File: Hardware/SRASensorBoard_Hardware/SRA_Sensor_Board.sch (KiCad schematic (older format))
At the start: 12 parts, among them U1 OKI-78SR-5_1.5-W36H-C, U2 OKI-78SR-3.3_1.5-W36H-C

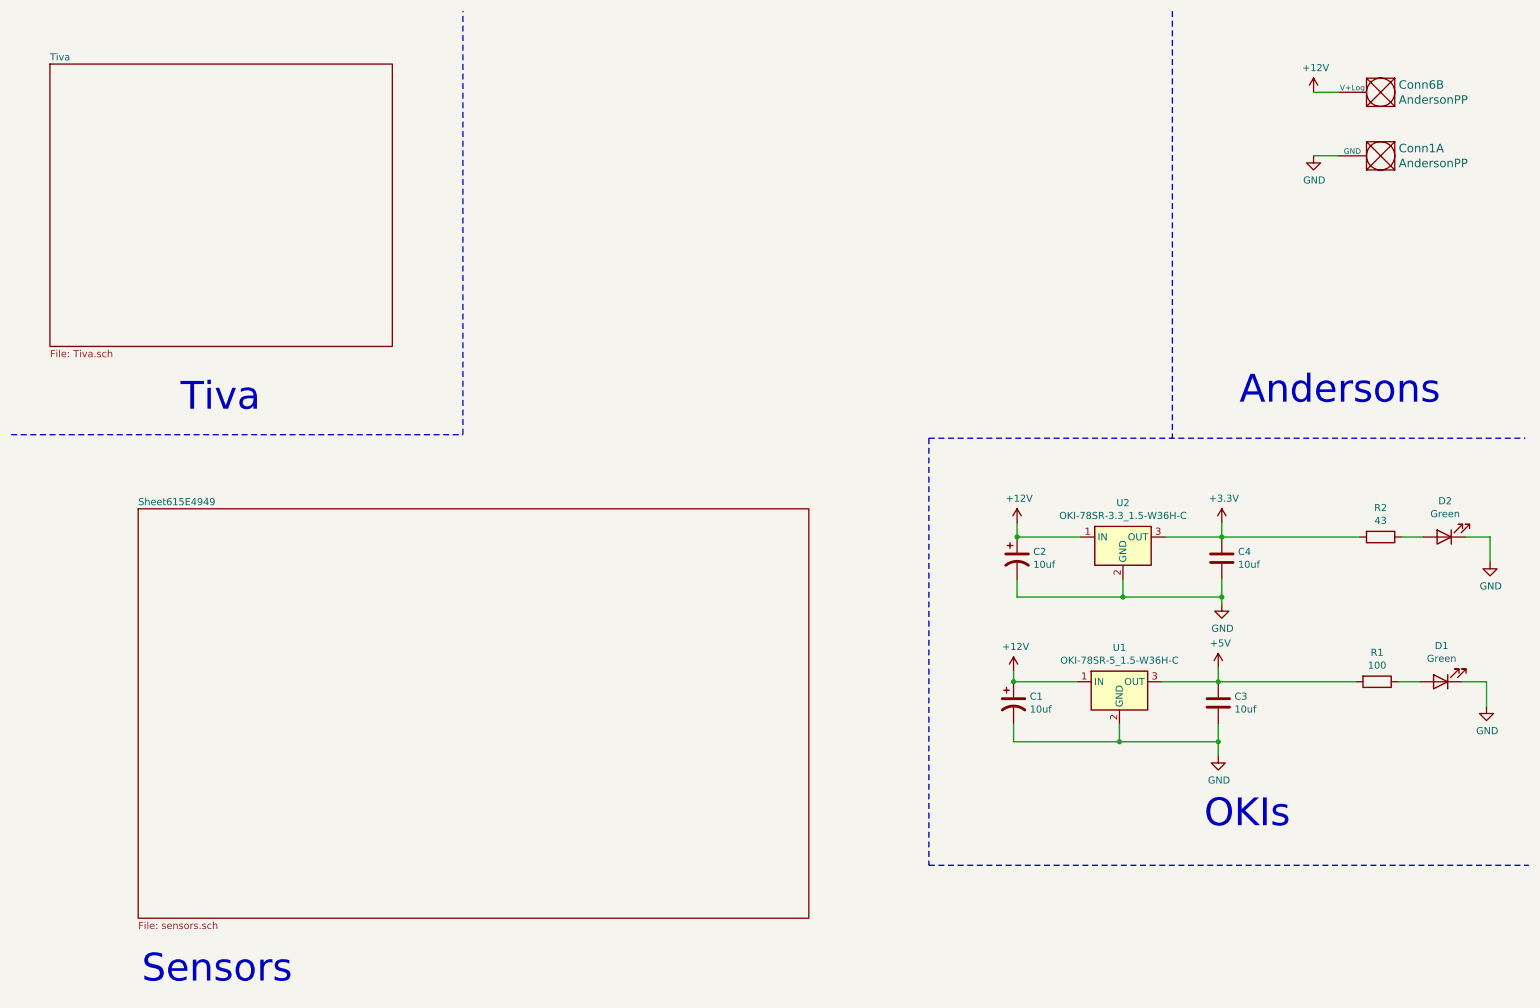
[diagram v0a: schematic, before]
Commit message: Science CDR changes
Changed NO to NO2, removed NH3 data lines for analog output and changed power to 5v, added 3 laser and photodiode pairs (mosfet not determined), added uv and lights connectors, updated tiva pins
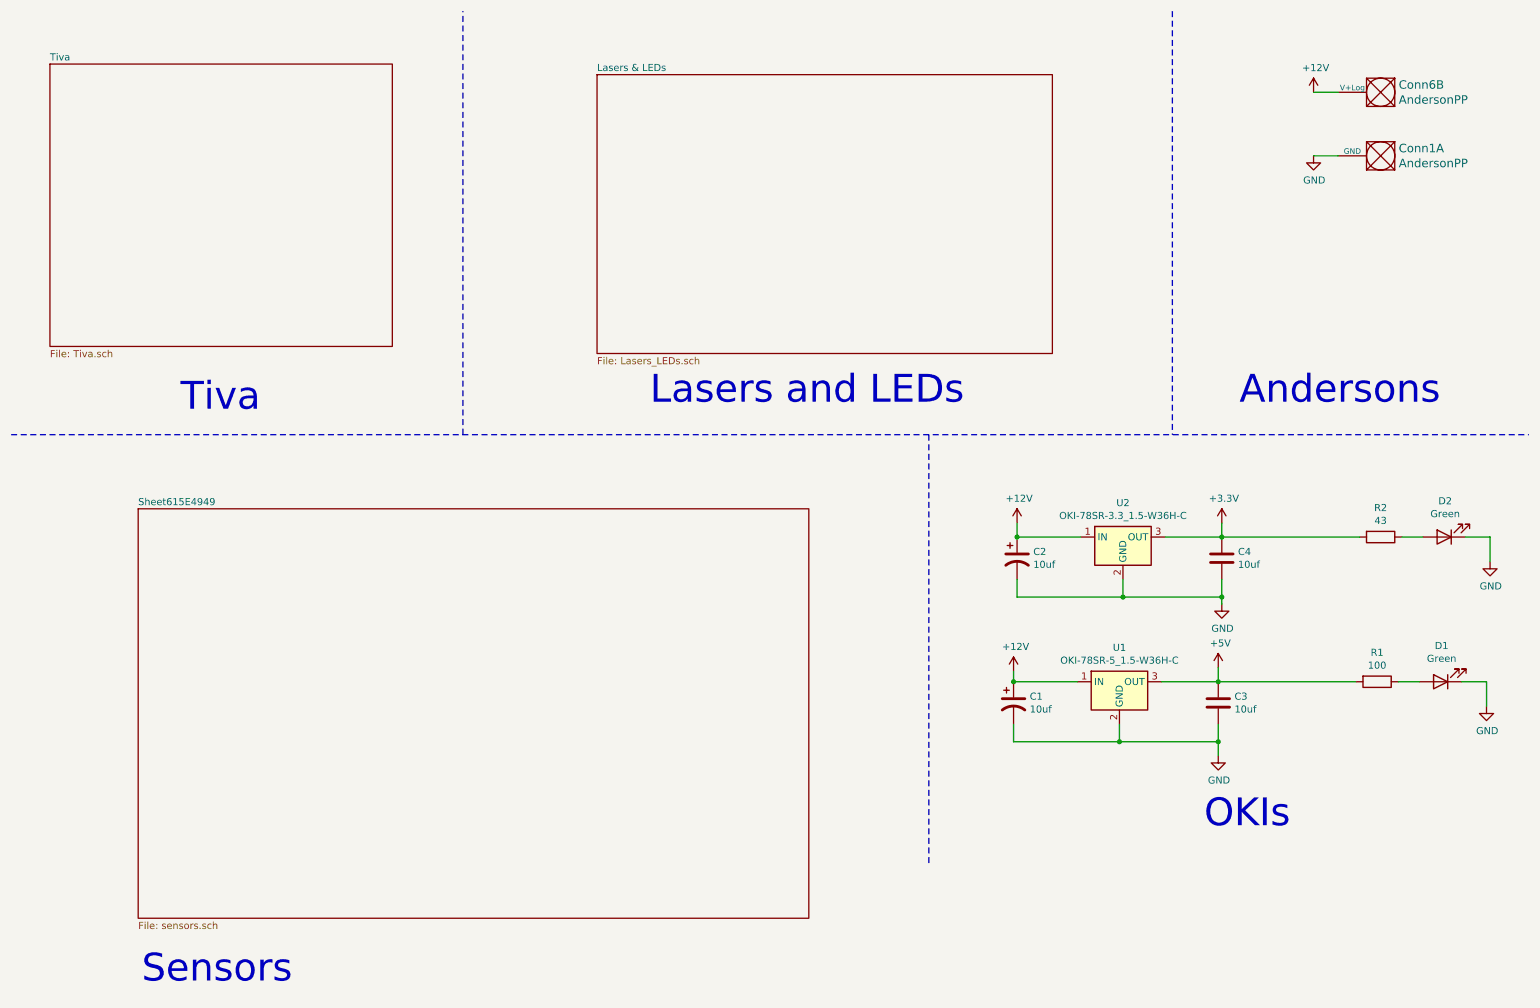
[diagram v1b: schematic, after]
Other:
- note added: "Lasers and LEDs"
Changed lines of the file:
@@
 $Descr A4 11693 8268
 encoding utf-8
-Sheet 1 3
+Sheet 1 4
 Title ""
 Date ""
@@
 $EndSheet
 Wire Notes Line
-	475  3475 3675 3475
-Wire Notes Line
 	3675 3475 3675 475
 Text Notes 1675 3325 0    197  ~ 0
 Tiva
 Wire Notes Line
-	8700 475  8700 3500
+	8700 475  8700 3475
 Text Notes 9175 3275 0    197  ~ 0
 Andersons
@@
 Sensors
 Wire Notes Line
-	6975 3500 6975 6525
-Wire Notes Line
-	6975 6525 11225 6525
-Wire Notes Line
-	6975 3500 11200 3500
+	6975 3475 6975 6525
 $Comp
 L Converter_DCDC:OKI-78SR-5_1.5-W36H-C U1
@@
 Wire Wire Line
 	9050 4200 10025 4200
+$Sheet
+S 4625 925  3225 1975
+U 61988F48
+F0 "Lasers & LEDs" 50
+F1 "Lasers_LEDs.sch" 50
+$EndSheet
+Text Notes 5000 3275 0    197  ~ 0
+Lasers and LEDs
+Wire Notes Line
+	475  3475 11225 3475
 $EndSCHEMATC

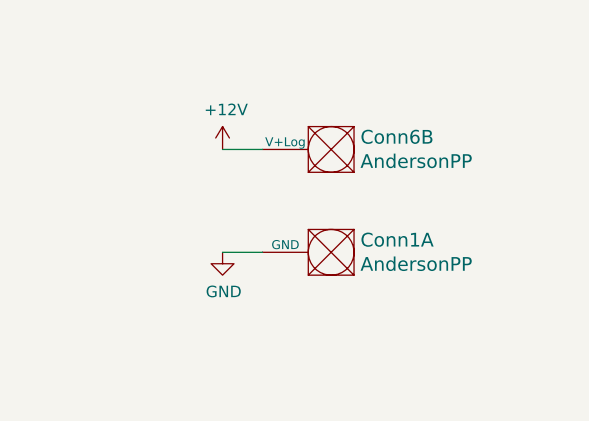
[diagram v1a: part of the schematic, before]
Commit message: added NO sensor stuff and finished layout
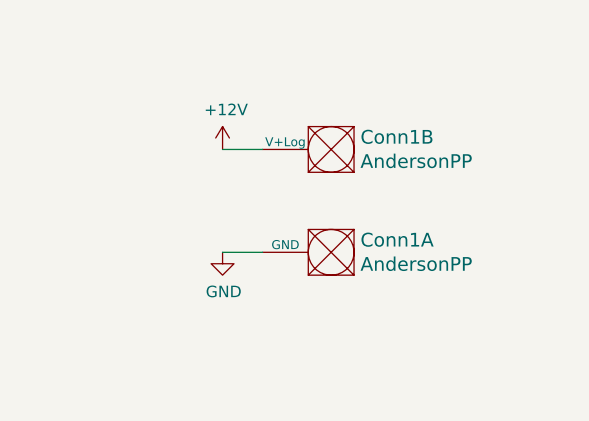
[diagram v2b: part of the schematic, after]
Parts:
- Conn1: renamed from Conn6; footprint MRDT_Connectors:Anderson_1_Horizontal -> MRDT_Connectors:Anderson_2_Horizontal_Side_by_Side
- Conn1: footprint MRDT_Connectors:Anderson_1_Horizontal -> MRDT_Connectors:Anderson_2_Horizontal_Side_by_Side
- R1: footprint Resistor_SMD:R_0402_1005Metric -> Resistor_SMD:R_0603_1608Metric_Pad0.98x0.95mm_HandSolder
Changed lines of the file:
@@
 $EndDescr
 $Comp
-L MRDT_Connectors:AndersonPP Conn6
+L MRDT_Connectors:AndersonPP Conn1
 U 2 1 614D19B3
 P 10275 950
-F 0 "Conn6" H 10247 997 60  0000 R CNN
+F 0 "Conn1" H 10247 997 60  0000 R CNN
 F 1 "AndersonPP" H 10247 1103 60  0000 R CNN
-F 2 "MRDT_Connectors:Anderson_1_Horizontal" H 10125 400 60  0001 C CNN
+F 2 "MRDT_Connectors:Anderson_2_Horizontal_Side_by_Side" H 10125 400 60  0001 C CNN
 F 3 "" H 10125 400 60  0001 C CNN
 	2    10275 950
@@
 F 0 "Conn1" H 10247 1447 60  0000 R CNN
 F 1 "AndersonPP" H 10247 1553 60  0000 R CNN
-F 2 "MRDT_Connectors:Anderson_1_Horizontal" H 10125 850 60  0001 C CNN
+F 2 "MRDT_Connectors:Anderson_2_Horizontal_Side_by_Side" H 10125 850 60  0001 C CNN
 F 3 "" H 10125 850 60  0001 C CNN
 	1    10275 1400
@@
 F 0 "R1" V 9943 5225 50  0000 C CNN
 F 1 "100" V 10034 5225 50  0000 C CNN
-F 2 "Resistor_SMD:R_0402_1005Metric" V 10080 5225 50  0001 C CNN
+F 2 "Resistor_SMD:R_0603_1608Metric_Pad0.98x0.95mm_HandSolder" V 10080 5225 50  0001 C CNN
 F 3 "~" H 10150 5225 50  0001 C CNN
 	1    10150 5225

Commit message: rev 2 changes
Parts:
- R1: value 100 -> 300
- R2: value 43 -> 130
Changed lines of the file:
@@
 P 10175 4200
 F 0 "R2" V 9968 4200 50  0000 C CNN
-F 1 "43" V 10059 4200 50  0000 C CNN
+F 1 "130" V 10059 4200 50  0000 C CNN
 F 2 "Resistor_SMD:R_0603_1608Metric_Pad1.05x0.95mm_HandSolder" V 10105 4200 50  0001 C CNN
 F 3 "~" H 10175 4200 50  0001 C CNN
@@
 P 10150 5225
 F 0 "R1" V 9943 5225 50  0000 C CNN
-F 1 "100" V 10034 5225 50  0000 C CNN
+F 1 "300" V 10034 5225 50  0000 C CNN
 F 2 "Resistor_SMD:R_0603_1608Metric_Pad0.98x0.95mm_HandSolder" V 10080 5225 50  0001 C CNN
 F 3 "~" H 10150 5225 50  0001 C CNN

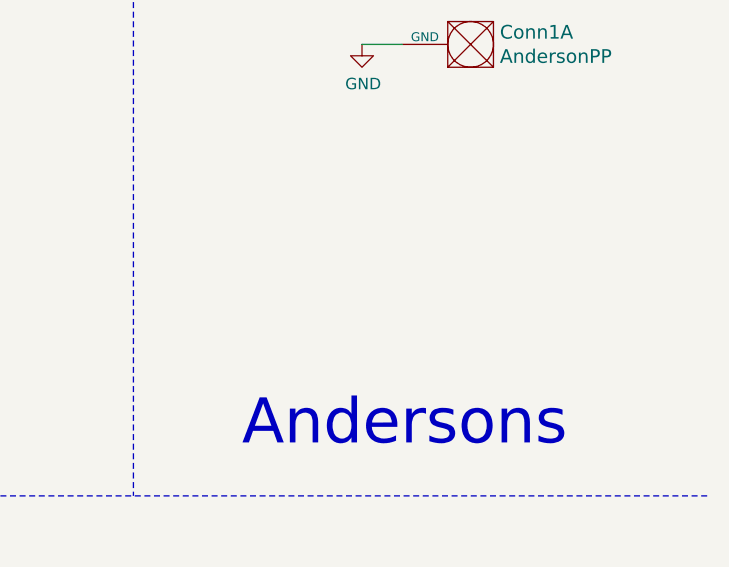
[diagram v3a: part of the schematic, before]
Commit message: added board mounts and did rev 2 changes
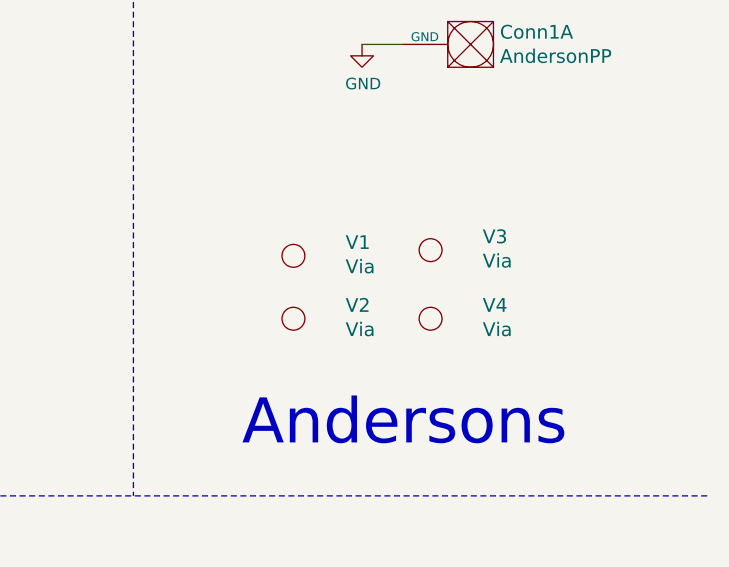
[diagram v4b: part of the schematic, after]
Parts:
- added V1, V2, V3, V4: Via, MRDT_Drill_Holes:4_40_Hole_Corner, symbol MRDT_Drill_Holes:Via
- C1: footprint Capacitor_SMD:C_0603_1608Metric_Pad1.05x0.95mm_HandSolder -> Capacitor_SMD:C_0603_1608Metric_Pad1.08x0.95mm_HandSolder
- R2: footprint Resistor_SMD:R_0603_1608Metric_Pad1.05x0.95mm_HandSolder -> Resistor_SMD:R_0603_1608Metric_Pad0.98x0.95mm_HandSolder
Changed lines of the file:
@@
 F 0 "R2" V 9968 4200 50  0000 C CNN
 F 1 "130" V 10059 4200 50  0000 C CNN
-F 2 "Resistor_SMD:R_0603_1608Metric_Pad1.05x0.95mm_HandSolder" V 10105 4200 50  0001 C CNN
+F 2 "Resistor_SMD:R_0603_1608Metric_Pad0.98x0.95mm_HandSolder" V 10105 4200 50  0001 C CNN
 F 3 "~" H 10175 4200 50  0001 C CNN
 	1    10175 4200
@@
 F 0 "C1" H 7690 5421 50  0000 L CNN
 F 1 "10uf" H 7690 5330 50  0000 L CNN
-F 2 "Capacitor_SMD:C_0603_1608Metric_Pad1.05x0.95mm_HandSolder" H 7575 5375 50  0001 C CNN
+F 2 "Capacitor_SMD:C_0603_1608Metric_Pad1.08x0.95mm_HandSolder" H 7575 5375 50  0001 C CNN
 F 3 "~" H 7575 5375 50  0001 C CNN
 	1    7575 5375
@@
 Wire Notes Line
 	475  3475 11225 3475
+$Comp
+L MRDT_Drill_Holes:Via V2
+U 1 1 622C1FEF
+P 9400 2700
+F 0 "V2" H 9628 2758 60  0000 L CNN
+F 1 "Via" H 9628 2652 60  0000 L CNN
+F 2 "MRDT_Drill_Holes:4_40_Hole_Corner" H 9400 2700 60  0001 C CNN
+F 3 "" H 9400 2700 60  0001 C CNN
+	1    9400 2700
+	1    0    0    -1
+$EndComp
+$Comp
+L MRDT_Drill_Holes:Via V1
+U 1 1 622C2C38
+P 9400 2425
+F 0 "V1" H 9628 2483 60  0000 L CNN
+F 1 "Via" H 9628 2377 60  0000 L CNN
+F 2 "MRDT_Drill_Holes:4_40_Hole_Corner" H 9400 2425 60  0001 C CNN
+F 3 "" H 9400 2425 60  0001 C CNN
+	1    9400 2425
+	1    0    0    -1
+$EndComp
+$Comp
+L MRDT_Drill_Holes:Via V3
+U 1 1 622C343B
+P 10000 2400
+F 0 "V3" H 10228 2458 60  0000 L CNN
+F 1 "Via" H 10228 2352 60  0000 L CNN
+F 2 "MRDT_Drill_Holes:4_40_Hole_Corner" H 10000 2400 60  0001 C CNN
+F 3 "" H 10000 2400 60  0001 C CNN
+	1    10000 2400
+	1    0    0    -1
+$EndComp
+$Comp
+L MRDT_Drill_Holes:Via V4
+U 1 1 622C3B50
+P 10000 2700
+F 0 "V4" H 10228 2758 60  0000 L CNN
+F 1 "Via" H 10228 2652 60  0000 L CNN
+F 2 "MRDT_Drill_Holes:4_40_Hole_Corner" H 10000 2700 60  0001 C CNN
+F 3 "" H 10000 2700 60  0001 C CNN
+	1    10000 2700
+	1    0    0    -1
+$EndComp
 $EndSCHEMATC
